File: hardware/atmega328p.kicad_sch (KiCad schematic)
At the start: 17 parts, among them U401 ATMEGA328P-PU, Y401 16MHz

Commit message: Added analog stage for Vbat measurement, and it's simulation
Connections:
- net VBAT: now reaches U401.24 (PC1)
- no-connect marks 6 -> 5
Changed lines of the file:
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@@
   (junction (at 110.49 143.51) (diameter 0) (color 0 0 0 0)
   )
-  (no_connect (at 128.27 95.25))
+  (no_connect (at 128.27 92.71))
   (no_connect (at 128.27 105.41))
-  (no_connect (at 128.27 92.71))
+  (no_connect (at 128.27 102.87))
   (no_connect (at 128.27 130.81))
-  (no_connect (at 128.27 102.87))
   (no_connect (at 128.27 123.19))
   (wire (pts (xy 146.05 99.06) (xy 146.05 97.79))
@@
     (effects (font (size 1.524 1.524)) (justify left bottom))
   )
+  (hierarchical_label "VBAT" (shape input) (at 128.27 95.25 0)
+    (effects (font (size 1.524 1.524)) (justify left))
+  )
   (hierarchical_label "PWM2" (shape input) (at 128.27 128.27 0)

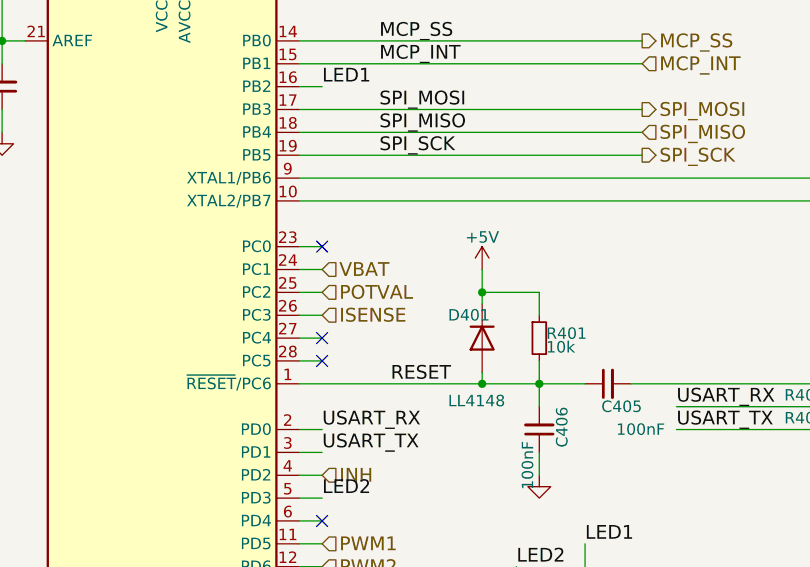
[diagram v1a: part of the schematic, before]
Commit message: hardware: K78L15 to supply INA826 and other changes
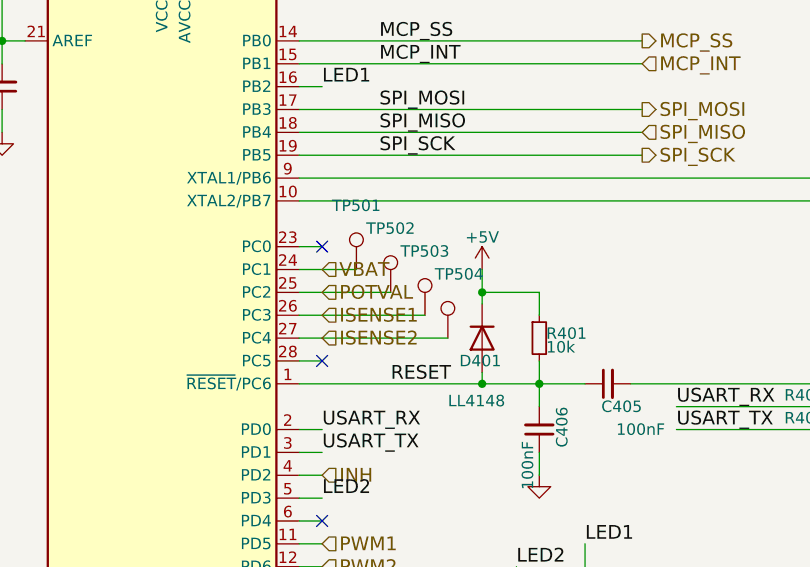
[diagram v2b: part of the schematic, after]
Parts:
- added TP501, TP502, TP503, TP504: (no value), symbol Connector:TestPoint
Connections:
- net POTVAL: now also TP502.1
- net VBAT: now also TP501.1
- net ISENSE2: now reaches U401.27 (PC4)
- net ISENSE2: now also TP504.1
- net ISENSE renamed ISENSE1
- net ISENSE1: now also TP503.1
- no-connect marks 5 -> 4
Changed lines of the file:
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@@
   (no_connect (at 128.27 92.71))
   (no_connect (at 128.27 105.41))
-  (no_connect (at 128.27 102.87))
   (no_connect (at 128.27 130.81))
   (no_connect (at 128.27 123.19))
@@
     (stroke (width 0) (type default) (color 0 0 0 0))
   )
+  (wire (pts (xy 125.73 97.79) (xy 135.89 97.79))
+    (stroke (width 0) (type default) (color 0 0 0 0))
+  )
+  (wire (pts (xy 125.73 102.87) (xy 142.24 102.87))
+    (stroke (width 0) (type default) (color 0 0 0 0))
+  )
   (wire (pts (xy 92.71 59.69) (xy 92.71 69.85))
     (stroke (width 0) (type default) (color 0 0 0 0))
@@
     (stroke (width 0) (type default) (color 0 0 0 0))
   )
+  (wire (pts (xy 125.73 95.25) (xy 132.08 95.25))
+    (stroke (width 0) (type default) (color 0 0 0 0))
+  )
   (wire (pts (xy 201.93 59.69) (xy 204.47 59.69))
     (stroke (width 0) (type default) (color 0 0 0 0))
   )
-  (wire (pts (xy 125.73 100.33) (xy 128.27 100.33))
-    (stroke (width 0) (type default) (color 0 0 0 0))
-  )
   (wire (pts (xy 152.4 107.95) (xy 152.4 110.49))
     (stroke (width 0) (type default) (color 0 0 0 0))
@@
     (stroke (width 0) (type default) (color 0 0 0 0))
   )
-  (wire (pts (xy 125.73 102.87) (xy 128.27 102.87))
-    (stroke (width 0) (type default) (color 0 0 0 0))
-  )
   (wire (pts (xy 210.82 101.6) (xy 217.17 101.6))
     (stroke (width 0) (type default) (color 0 0 0 0))
@@
     (stroke (width 0) (type default) (color 0 0 0 0))
   )
+  (wire (pts (xy 125.73 100.33) (xy 139.7 100.33))
+    (stroke (width 0) (type default) (color 0 0 0 0))
+  )
   (wire (pts (xy 125.73 85.09) (xy 217.17 85.09))
     (stroke (width 0) (type default) (color 0 0 0 0))
@@
     (stroke (width 0) (type default) (color 0 0 0 0))
   )
-  (wire (pts (xy 128.27 95.25) (xy 125.73 95.25))
-    (stroke (width 0) (type default) (color 0 0 0 0))
-  )
   (wire (pts (xy 125.73 77.47) (xy 163.83 77.47))
     (stroke (width 0) (type default) (color 0 0 0 0))
@@
   )
   (wire (pts (xy 113.03 62.23) (xy 113.03 59.69))
-    (stroke (width 0) (type default) (color 0 0 0 0))
-  )
-  (wire (pts (xy 125.73 97.79) (xy 128.27 97.79))
     (stroke (width 0) (type default) (color 0 0 0 0))
   )
@@
     (effects (font (size 1.524 1.524)) (justify right))
   )
+  (hierarchical_label "ISENSE2" (shape input) (at 128.27 102.87 0)
+    (effects (font (size 1.524 1.524)) (justify left))
+  )
   (hierarchical_label "MCP_INT" (shape input) (at 163.83 72.39 0)
     (effects (font (size 1.524 1.524)) (justify left))
@@
     (effects (font (size 1.524 1.524)) (justify left))
   )
-  (hierarchical_label "ISENSE" (shape input) (at 128.27 100.33 0)
+  (hierarchical_label "ISENSE1" (shape input) (at 128.27 100.33 0)
     (effects (font (size 1.524 1.524)) (justify left))
   )
@@
   (symbol (lib_id "Diode:LL4148") (at 146.05 102.87 90) (mirror x) (unit 1)
     (in_bom yes) (on_board yes)
-    (property "Reference" "D401" (id 0) (at 142.24 100.33 90)
+    (property "Reference" "D401" (id 0) (at 143.51 105.41 90)
       (effects (font (size 1.27 1.27)) (justify right))
     )
@@
     (pin "1")
   )
+  (symbol (lib_id "Connector:TestPoint") (at 135.89 97.79 0) (unit 1)
+    (in_bom yes) (on_board yes)
+    (property "Reference" "TP502" (id 0) (at 135.89 91.44 0)
+      (effects (font (size 1.27 1.27)) (justify bottom))
+    )
+    (property "Value" "" (id 1) (at 135.89 92.71 0))
+    (property "Footprint" "" (id 2) (at 135.89 97.79 0)
+      (effects (font (size 1.27 1.27)) hide)
+    )
+    (property "Datasheet" "" (id 3) (at 135.89 97.79 0)
+      (effects (font (size 1.27 1.27)) hide)
+    )
+    (pin "1")
+  )
+  (symbol (lib_id "Connector:TestPoint") (at 142.24 102.87 0) (unit 1)
+    (in_bom yes) (on_board yes)
+    (property "Reference" "TP504" (id 0) (at 143.51 96.52 0)
+      (effects (font (size 1.27 1.27)) (justify bottom))
+    )
+    (property "Value" "" (id 1) (at 143.51 97.79 0))
+    (property "Footprint" "" (id 2) (at 142.24 102.87 0)
+      (effects (font (size 1.27 1.27)) hide)
+    )
+    (property "Datasheet" "" (id 3) (at 142.24 102.87 0)
+      (effects (font (size 1.27 1.27)) hide)
+    )
+    (pin "1")
+  )
   (symbol (lib_id "power:+5V") (at 110.49 44.45 0) (unit 1)
     (in_bom yes) (on_board yes) (fields_autoplaced)
@@
     (pin "1")
   )
+  (symbol (lib_id "Connector:TestPoint") (at 132.08 95.25 0) (unit 1)
+    (in_bom yes) (on_board yes)
+    (property "Reference" "TP501" (id 0) (at 132.08 88.9 0)
+      (effects (font (size 1.27 1.27)) (justify bottom))
+    )
+    (property "Value" "" (id 1) (at 132.08 90.17 0))
+    (property "Footprint" "" (id 2) (at 132.08 95.25 0)
+      (effects (font (size 1.27 1.27)) hide)
+    )
+    (property "Datasheet" "" (id 3) (at 132.08 95.25 0)
+      (effects (font (size 1.27 1.27)) hide)
+    )
+    (pin "1")
+  )
   (symbol (lib_id "power:+5V") (at 204.47 54.61 0) (unit 1)
     (in_bom yes) (on_board yes) (fields_autoplaced)
@@
       (effects (font (size 1.27 1.27)) hide)
     )
+    (pin "1")
+  )
+  (symbol (lib_id "Connector:TestPoint") (at 139.7 100.33 0) (unit 1)
+    (in_bom yes) (on_board yes)
+    (property "Reference" "TP503" (id 0) (at 139.7 93.98 0)
+      (effects (font (size 1.27 1.27)) (justify bottom))
+    )
+    (property "Value" "" (id 1) (at 139.7 95.25 0))
+    (property "Footprint" "" (id 2) (at 139.7 100.33 0)
+      (effects (font (size 1.27 1.27)) hide)
+    )
+    (property "Datasheet" "" (id 3) (at 139.7 100.33 0)
+      (effects (font (size 1.27 1.27)) hide)
+    )

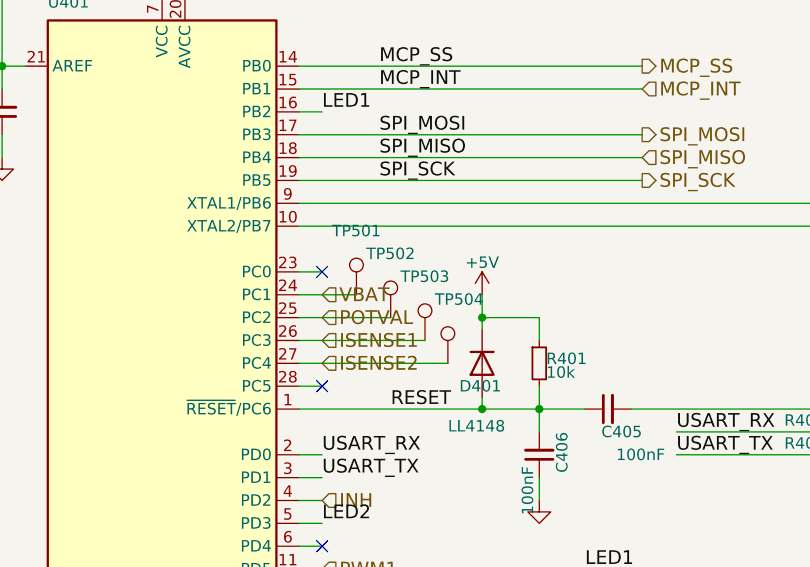
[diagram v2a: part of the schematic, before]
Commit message: hardware: silkscreen updated with JLC. Finished.
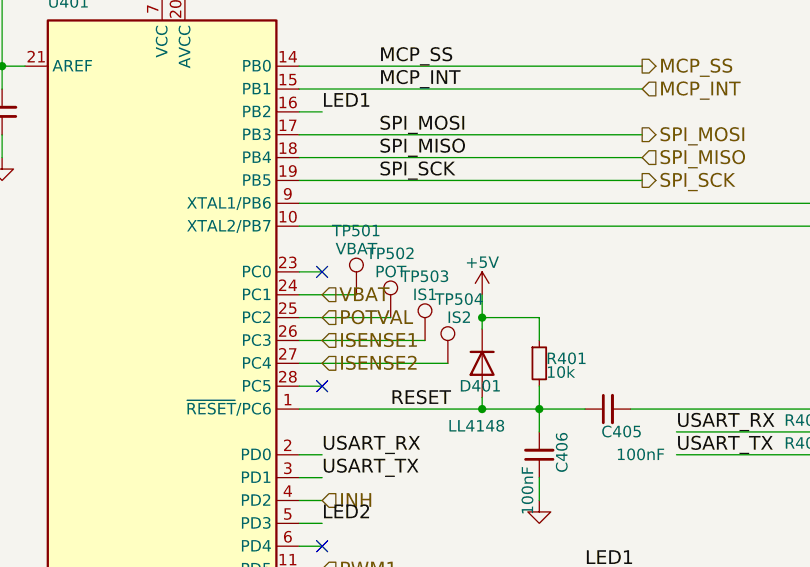
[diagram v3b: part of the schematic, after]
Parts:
- TP501: value (none) -> VBAT; footprint (none) -> TestPoint:TestPoint_Pad_2.0x2.0mm
- TP502: value (none) -> POT; footprint (none) -> TestPoint:TestPoint_Pad_2.0x2.0mm
- TP503: value (none) -> IS1; footprint (none) -> TestPoint:TestPoint_Pad_2.0x2.0mm
- TP504: value (none) -> IS2; footprint (none) -> TestPoint:TestPoint_Pad_2.0x2.0mm
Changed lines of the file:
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@@
       (effects (font (size 1.27 1.27)) (justify bottom))
     )
-    (property "Value" "" (id 1) (at 135.89 92.71 0))
-    (property "Footprint" "" (id 2) (at 135.89 97.79 0)
+    (property "Value" "POT" (id 1) (at 135.89 92.71 0))
+    (property "Footprint" "TestPoint:TestPoint_Pad_2.0x2.0mm" (id 2) (at 135.89 97.79 0)
       (effects (font (size 1.27 1.27)) hide)
     )
@@
       (effects (font (size 1.27 1.27)) (justify bottom))
     )
-    (property "Value" "" (id 1) (at 143.51 97.79 0))
-    (property "Footprint" "" (id 2) (at 142.24 102.87 0)
+    (property "Value" "IS2" (id 1) (at 143.51 97.79 0))
+    (property "Footprint" "TestPoint:TestPoint_Pad_2.0x2.0mm" (id 2) (at 142.24 102.87 0)
       (effects (font (size 1.27 1.27)) hide)
     )
@@
       (effects (font (size 1.27 1.27)) (justify bottom))
     )
-    (property "Value" "" (id 1) (at 132.08 90.17 0))
-    (property "Footprint" "" (id 2) (at 132.08 95.25 0)
+    (property "Value" "VBAT" (id 1) (at 132.08 90.17 0))
+    (property "Footprint" "TestPoint:TestPoint_Pad_2.0x2.0mm" (id 2) (at 132.08 95.25 0)
       (effects (font (size 1.27 1.27)) hide)
     )
@@
       (effects (font (size 1.27 1.27)) (justify bottom))
     )
-    (property "Value" "" (id 1) (at 139.7 95.25 0))
-    (property "Footprint" "" (id 2) (at 139.7 100.33 0)
+    (property "Value" "IS1" (id 1) (at 139.7 95.25 0))
+    (property "Footprint" "TestPoint:TestPoint_Pad_2.0x2.0mm" (id 2) (at 139.7 100.33 0)
       (effects (font (size 1.27 1.27)) hide)
     )
